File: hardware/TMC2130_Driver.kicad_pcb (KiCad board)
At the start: 2 copper layers, 36.7 x 39.4 mm, 35 parts, among them J1 PCIe_Stepper, J2 Conn_01x04_Male, J3 Screw_Terminal_01x02, U1 TMC2130, U2 24LC02

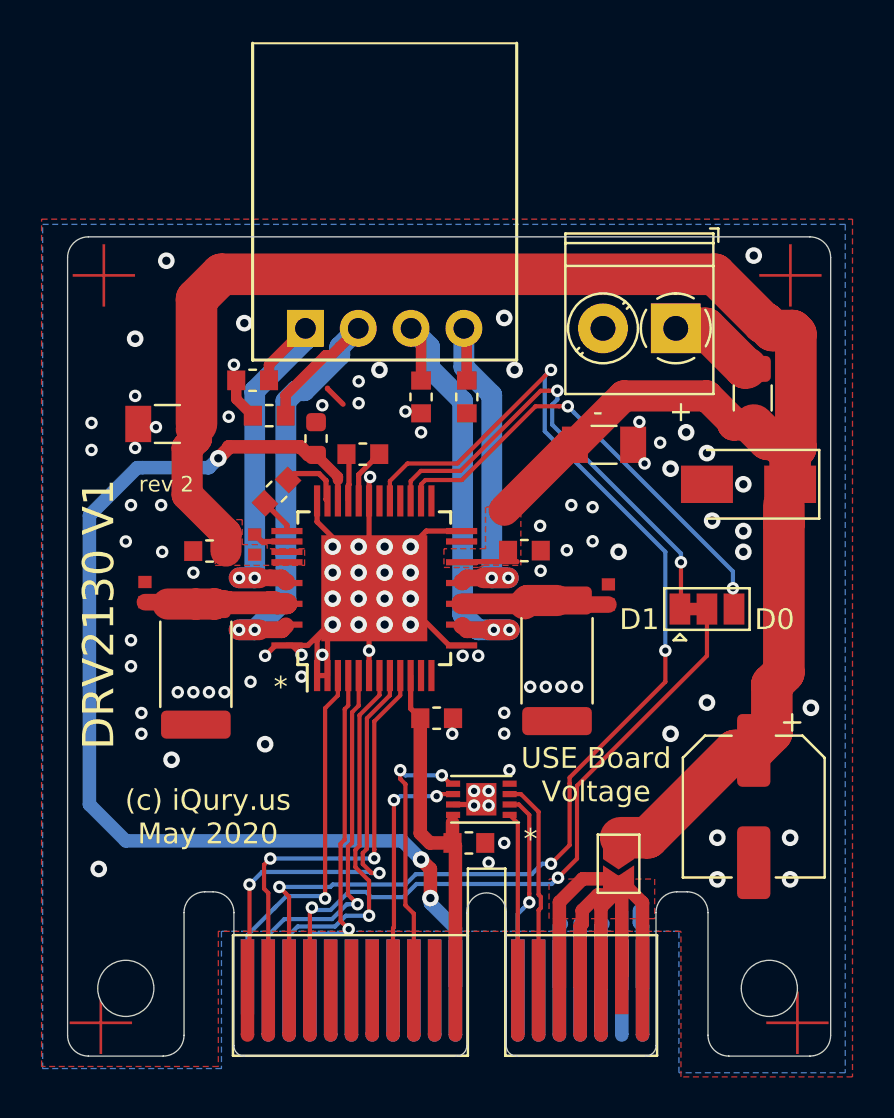
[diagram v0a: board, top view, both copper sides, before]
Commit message: Added external clock source and routed it to the Stepper. Make the TMC2130 use the external clock.
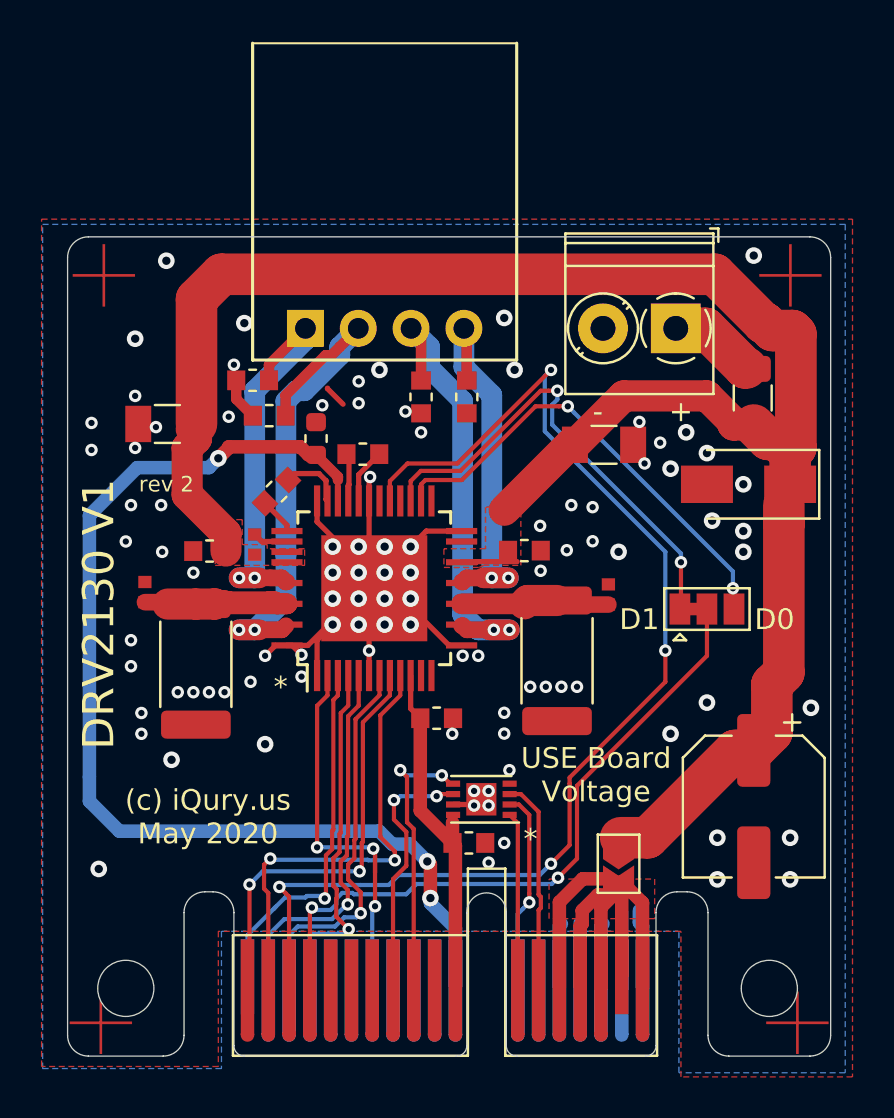
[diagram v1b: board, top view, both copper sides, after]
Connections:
- J1 pad : (no net) -> /STEP
- J1 pad A7: (no net) -> /CLOCK
- U1 pad 2: GND -> /CLOCK
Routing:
- net /CLOCK: track 0.00 -> 18.8 mm, vias 0 -> 3
- net GND: track 65.3 -> 59.7 mm, vias 98 -> 97
- net /STEP: track 22.1 -> 20.6 mm
- net /DIR: track 20.7 -> 22.0 mm
- net /V_IO: track 17.9 -> 17.2 mm

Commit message: Updated driver PCBs.
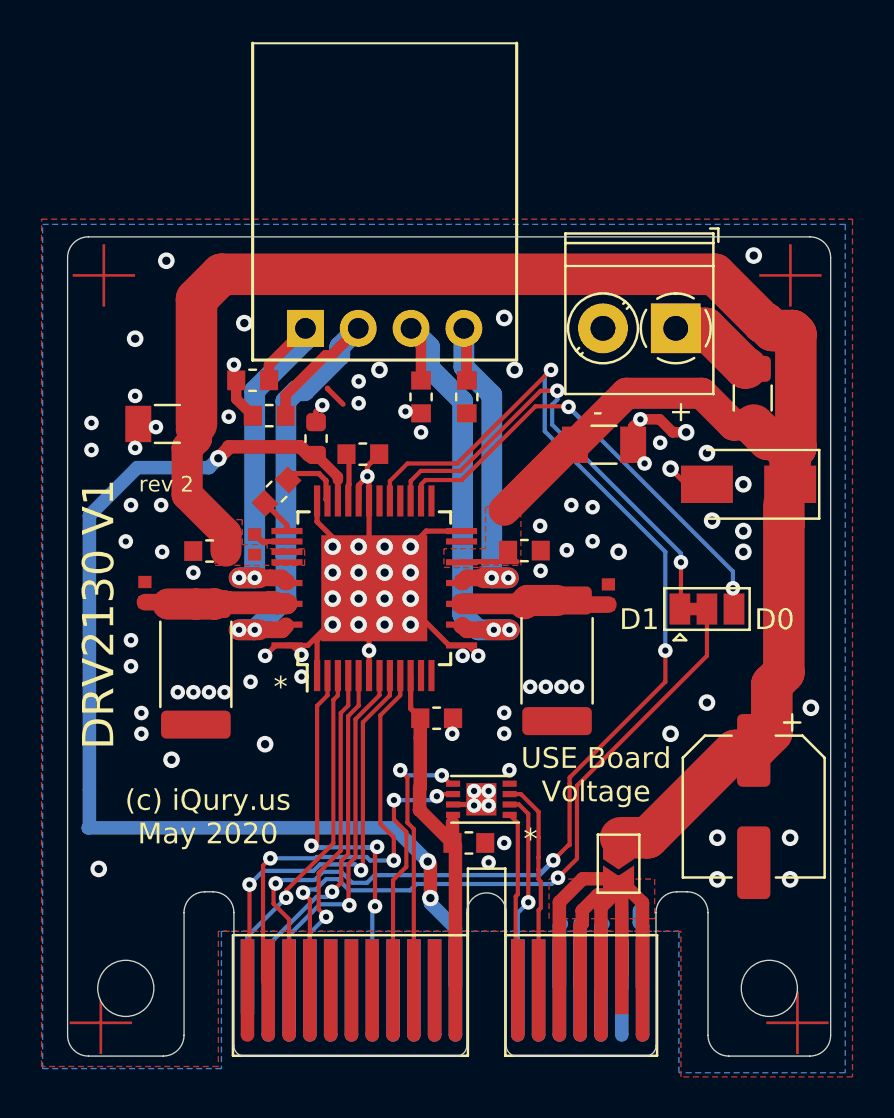
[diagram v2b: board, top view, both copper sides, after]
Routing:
- net GND: track 59.7 -> 69.1 mm
- net /CLOCK: track 18.8 -> 20.7 mm
- net /~ENABLE: track 58.0 -> 59.8 mm
- net /~CS: track 17.7 -> 16.3 mm
- net /SCK: track 17.3 -> 16.0 mm
- net /ALARM1: track 32.5 -> 33.6 mm
- net /MISO: track 18.7 -> 17.7 mm
- net /5V: track 52.9 -> 53.7 mm
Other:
- rule via_min_size: 0.508 -> 0.2

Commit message: Update to the latest daily Kicad. Fix board outline issue on PrntrBoardV2.
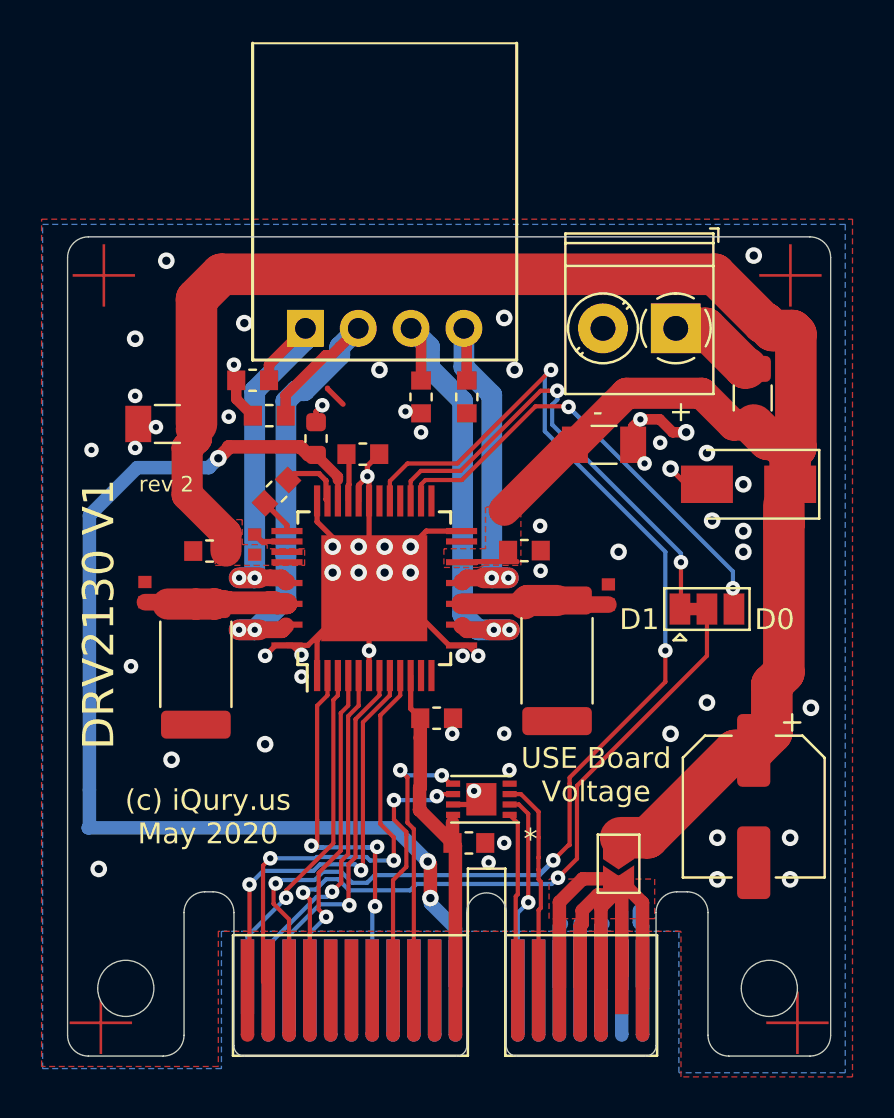
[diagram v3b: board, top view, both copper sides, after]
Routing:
- net GND: vias 97 -> 61
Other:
- net class Default removed

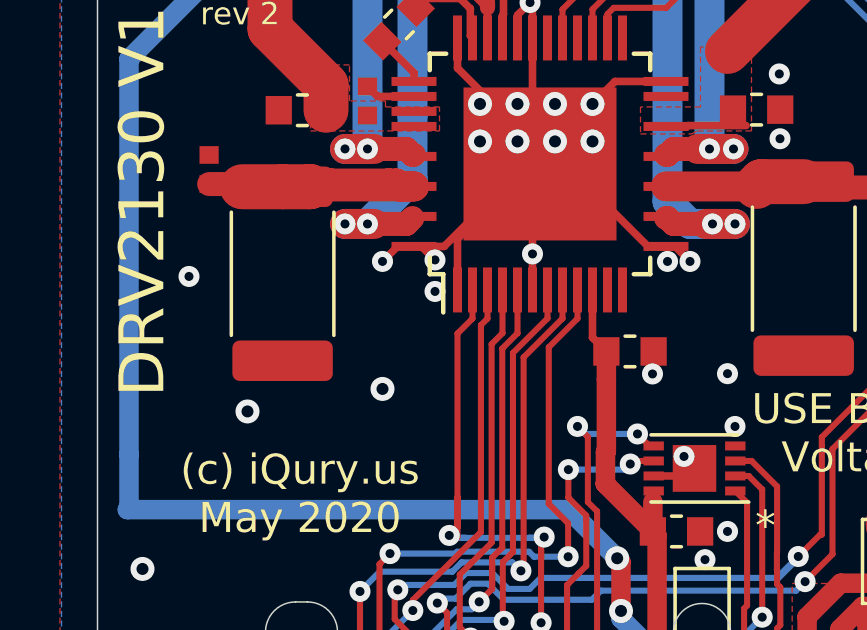
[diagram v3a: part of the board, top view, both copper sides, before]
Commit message: Updated DRC rules. Fix labels.
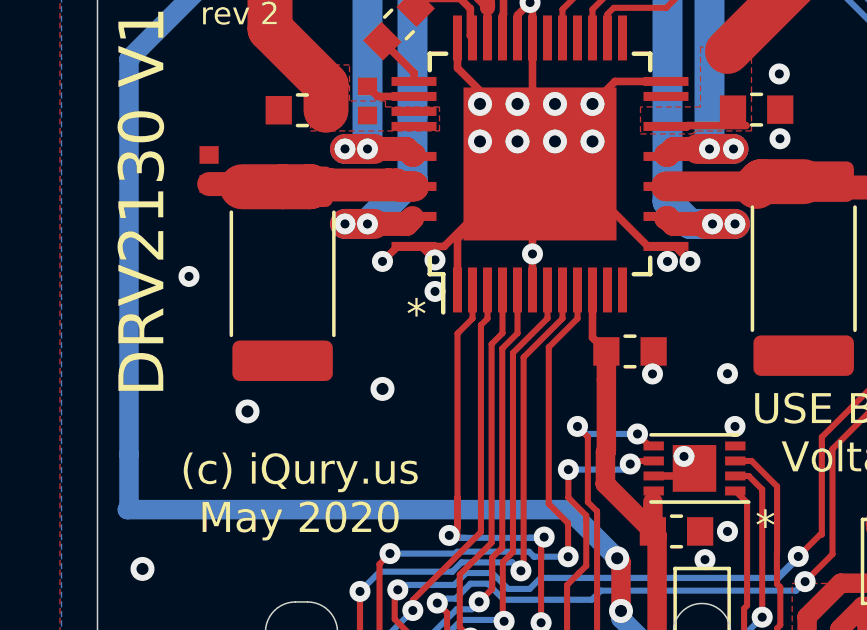
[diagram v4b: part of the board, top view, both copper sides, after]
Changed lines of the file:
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@@
     (pcbplotparams
       (layerselection 0x00010fc_ffffffff)
+      (disableapertmacros false)
       (usegerberextensions true)
       (usegerberattributes false)
@@
       (svgprecision 6)
       (excludeedgelayer true)
-      (linewidth 0.100000)
       (plotframeref false)
       (viasonmask false)
@@
     (effects (font (size 1 1) (thickness 0.15)))
   )
+  (gr_text "*" (at 119.634 96.52) (layer "F.SilkS")
+    (effects (font (size 1 1) (thickness 0.15)))
+  )

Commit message: Update 2660 and 2130 driver fab files.
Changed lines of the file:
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@@
     (fp_line (start 3.15 1.6) (end -3.15 1.6) (layer "F.Fab") (width 0.1))
     (fp_line (start 3.15 -1.6) (end 3.15 1.6) (layer "F.Fab") (width 0.1))
-    (pad "1" smd roundrect (at -2.9 0 270) (size 1.35 3.35) (layers "F.Cu" "F.Paste" "F.Mask") (roundrect_rratio 0.185185)
+    (pad "1" smd roundrect (at -2.9 0 270) (size 1.35 3.35) (layers "F.Cu" "F.Paste" "F.Mask") (roundrect_rratio 0.1851851851851852)
       (net 20 "Net-(C10-Pad1)"))
-    (pad "2" smd roundrect (at 2.9 0 270) (size 1.35 3.35) (layers "F.Cu" "F.Paste" "F.Mask") (roundrect_rratio 0.185185)
+    (pad "2" smd roundrect (at 2.9 0 270) (size 1.35 3.35) (layers "F.Cu" "F.Paste" "F.Mask") (roundrect_rratio 0.1851851851851852)
       (net 2 "GND"))
     (model "${KISYS3DMOD}/Resistor_SMD.3dshapes/R_2512_6332Metric.wrl"
@@
     (fp_line (start 3.15 -1.6) (end 3.15 1.6) (layer "F.Fab") (width 0.1))
     (fp_line (start -3.15 1.6) (end -3.15 -1.6) (layer "F.Fab") (width 0.1))
-    (pad "1" smd roundrect (at -2.9 0 270) (size 1.35 3.35) (layers "F.Cu" "F.Paste" "F.Mask") (roundrect_rratio 0.185185)
+    (pad "1" smd roundrect (at -2.9 0 270) (size 1.35 3.35) (layers "F.Cu" "F.Paste" "F.Mask") (roundrect_rratio 0.1851851851851852)
       (net 21 "Net-(C15-Pad1)"))
-    (pad "2" smd roundrect (at 2.9 0 270) (size 1.35 3.35) (layers "F.Cu" "F.Paste" "F.Mask") (roundrect_rratio 0.185185)
+    (pad "2" smd roundrect (at 2.9 0 270) (size 1.35 3.35) (layers "F.Cu" "F.Paste" "F.Mask") (roundrect_rratio 0.1851851851851852)
       (net 2 "GND"))
     (model "${KISYS3DMOD}/Resistor_SMD.3dshapes/R_2512_6332Metric.wrl"
@@
           (xy 0.5 0.75)
           (xy -0.5 0.75)
-) (width 0))
+        ) (width 0))
       ))
     (pad "2" smd custom (at 0.725 0 270) (size 0.3 0.3) (layers "F.Cu" "F.Mask")
@@
           (xy -0.65 0.75)
           (xy -0.15 0)
-) (width 0))
+        ) (width 0))
       ))
   )

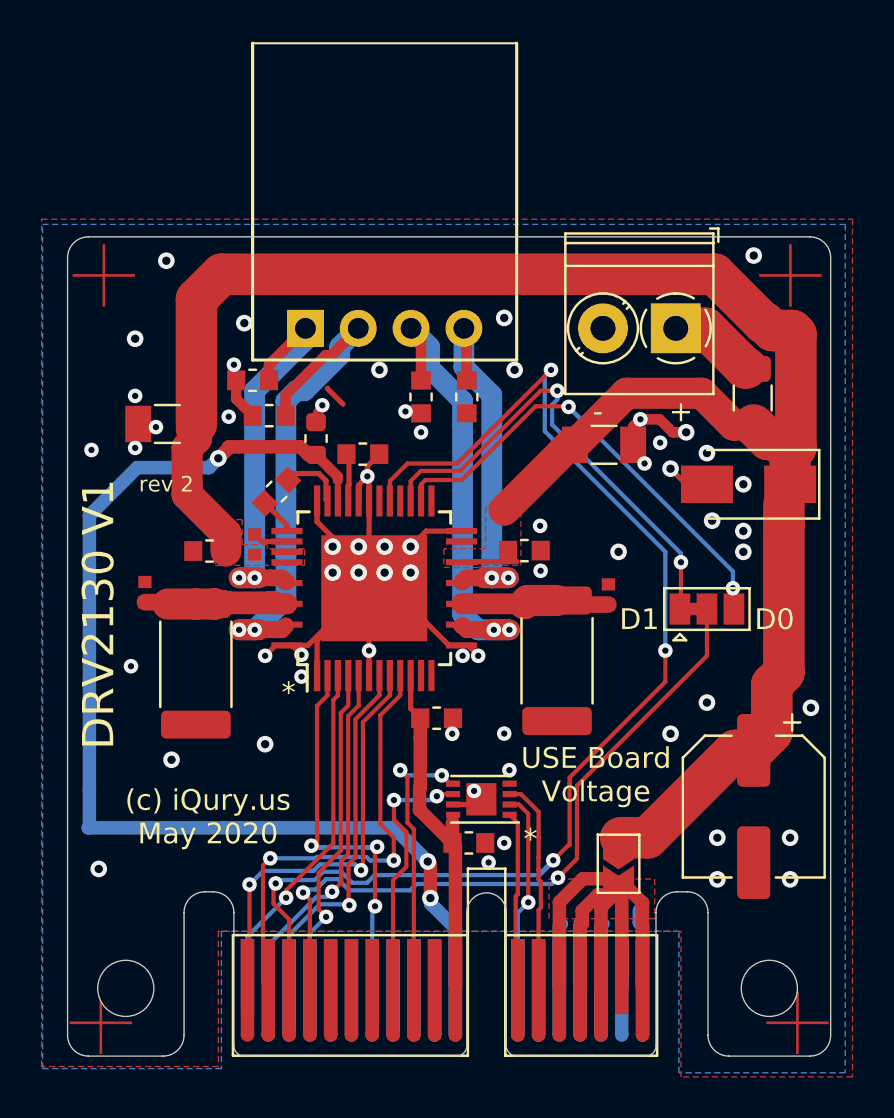
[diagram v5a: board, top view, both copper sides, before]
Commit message: Update of PCBs
- added tooling holes
- added order number location under components

Updated projects:
- DRV-Stepstick
- TMC2209
- TMC2130
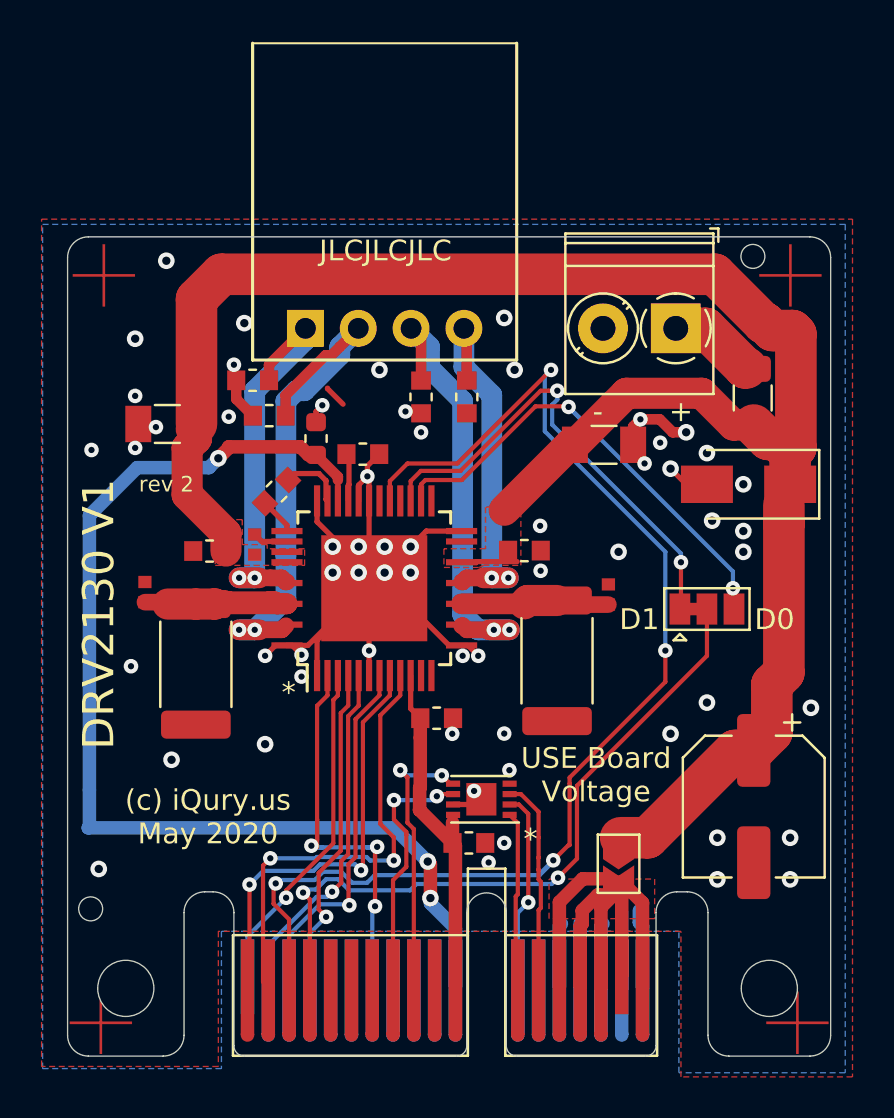
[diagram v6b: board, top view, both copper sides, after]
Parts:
- added H3: JLC Tooling Hole, PrntrBoardV2:JLC_Tool_hole, F.Cu at (105.5, 110.2)
- added H4: JLC Tooling Hole, PrntrBoardV2:JLC_Tool_hole, F.Cu at (103.4, 110.2)
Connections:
- J1 pad : /STEP -> (no net)
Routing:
- net GND: vias 61 -> 60
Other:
- board text added: "JLCJLCJLC"
